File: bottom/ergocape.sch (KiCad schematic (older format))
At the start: 10 parts

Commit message: cleanup and finish the case files
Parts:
- H1, H10, H11, H12, H2, H3, H5, H6, H8, H9: footprint usbc_footprint:mount_hole_2.4x4 -> acheron_MountingHoles:MountingHole_2.5x4.0mm
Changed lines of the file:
@@
 F 0 "H5" H 1100 4996 50  0000 L CNN
 F 1 "MountingHole" H 1100 4905 50  0000 L CNN
-F 2 "usbc_footprint:mount_hole_2.4x4" H 1000 4950 50  0001 C CNN
+F 2 "acheron_MountingHoles:MountingHole_2.5x4.0mm" H 1000 4950 50  0001 C CNN
 F 3 "~" H 1000 4950 50  0001 C CNN
 	1    1000 4950
@@
 F 0 "H12" H 1550 4996 50  0000 L CNN
 F 1 "MountingHole" H 1550 4905 50  0000 L CNN
-F 2 "usbc_footprint:mount_hole_2.4x4" H 1450 4950 50  0001 C CNN
+F 2 "acheron_MountingHoles:MountingHole_2.5x4.0mm" H 1450 4950 50  0001 C CNN
 F 3 "~" H 1450 4950 50  0001 C CNN
 	1    1450 4950
@@
 F 0 "H6" H 1100 5246 50  0000 L CNN
 F 1 "MountingHole" H 1100 5155 50  0000 L CNN
-F 2 "usbc_footprint:mount_hole_2.4x4" H 1000 5200 50  0001 C CNN
+F 2 "acheron_MountingHoles:MountingHole_2.5x4.0mm" H 1000 5200 50  0001 C CNN
 F 3 "~" H 1000 5200 50  0001 C CNN
 	1    1000 5200
@@
 F 0 "H11" H 1550 5246 50  0000 L CNN
 F 1 "MountingHole" H 1550 5155 50  0000 L CNN
-F 2 "usbc_footprint:mount_hole_2.4x4" H 1450 5200 50  0001 C CNN
+F 2 "acheron_MountingHoles:MountingHole_2.5x4.0mm" H 1450 5200 50  0001 C CNN
 F 3 "~" H 1450 5200 50  0001 C CNN
 	1    1450 5200
@@
 F 0 "H10" H 1550 5496 50  0000 L CNN
 F 1 "MountingHole" H 1550 5405 50  0000 L CNN
-F 2 "usbc_footprint:mount_hole_2.4x4" H 1450 5450 50  0001 C CNN
+F 2 "acheron_MountingHoles:MountingHole_2.5x4.0mm" H 1450 5450 50  0001 C CNN
 F 3 "~" H 1450 5450 50  0001 C CNN
 	1    1450 5450
@@
 F 0 "H8" H 1100 5746 50  0000 L CNN
 F 1 "MountingHole" H 1100 5655 50  0000 L CNN
-F 2 "usbc_footprint:mount_hole_2.4x4" H 1000 5700 50  0001 C CNN
+F 2 "acheron_MountingHoles:MountingHole_2.5x4.0mm" H 1000 5700 50  0001 C CNN
 F 3 "~" H 1000 5700 50  0001 C CNN
 	1    1000 5700
@@
 F 0 "H9" H 1550 5746 50  0000 L CNN
 F 1 "MountingHole" H 1550 5655 50  0000 L CNN
-F 2 "usbc_footprint:mount_hole_2.4x4" H 1450 5700 50  0001 C CNN
+F 2 "acheron_MountingHoles:MountingHole_2.5x4.0mm" H 1450 5700 50  0001 C CNN
 F 3 "~" H 1450 5700 50  0001 C CNN
 	1    1450 5700
@@
 F 0 "H1" H 1100 4546 50  0000 L CNN
 F 1 "MountingHole" H 1100 4455 50  0000 L CNN
-F 2 "usbc_footprint:mount_hole_2.4x4" H 1000 4500 50  0001 C CNN
+F 2 "acheron_MountingHoles:MountingHole_2.5x4.0mm" H 1000 4500 50  0001 C CNN
 F 3 "~" H 1000 4500 50  0001 C CNN
 	1    1000 4500
@@
 F 0 "H2" H 1550 4546 50  0000 L CNN
 F 1 "MountingHole" H 1550 4455 50  0000 L CNN
-F 2 "usbc_footprint:mount_hole_2.4x4" H 1450 4500 50  0001 C CNN
+F 2 "acheron_MountingHoles:MountingHole_2.5x4.0mm" H 1450 4500 50  0001 C CNN
 F 3 "~" H 1450 4500 50  0001 C CNN
 	1    1450 4500
@@
 F 0 "H3" H 1100 4796 50  0000 L CNN
 F 1 "MountingHole" H 1100 4705 50  0000 L CNN
-F 2 "usbc_footprint:mount_hole_2.4x4" H 1000 4750 50  0001 C CNN
+F 2 "acheron_MountingHoles:MountingHole_2.5x4.0mm" H 1000 4750 50  0001 C CNN
 F 3 "~" H 1000 4750 50  0001 C CNN
 	1    1000 4750

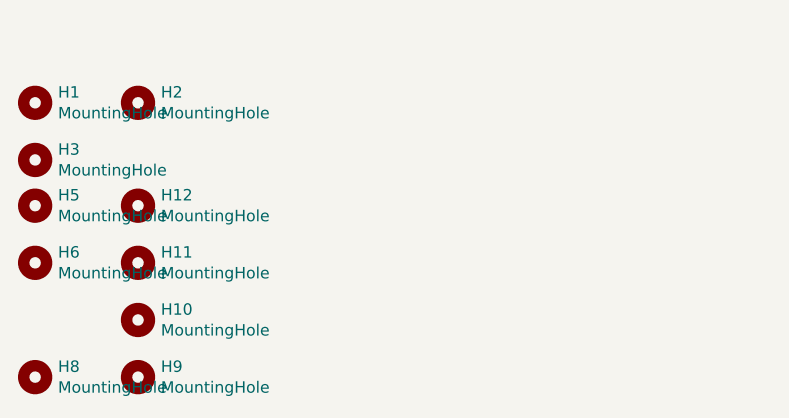
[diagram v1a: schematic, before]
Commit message: finalize plate and mounting holes
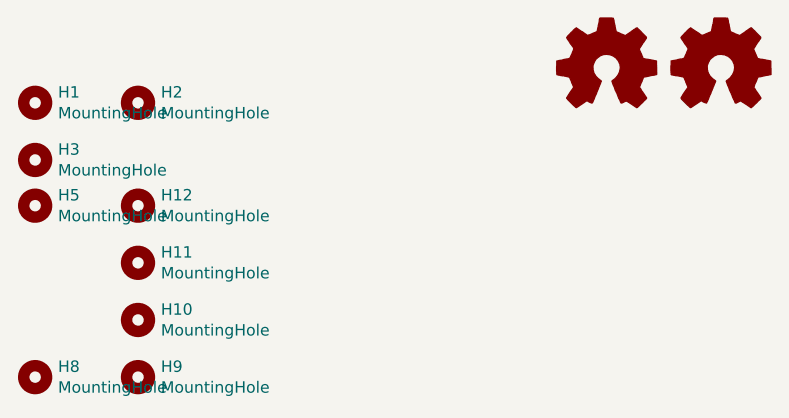
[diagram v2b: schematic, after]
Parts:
- removed H6: MountingHole, acheron_MountingHoles:MountingHole_2.5x4.0mm, symbol Mechanical:MountingHole
- H1, H10, H11, H12, H2, H3, H5, H8, H9: footprint acheron_MountingHoles:MountingHole_2.5x4.0mm -> MountingHole:MountingHole_2.7mm_M2.5
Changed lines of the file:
@@
 EESchema Schematic File Version 4
-LIBS:ergocape-cache
-EELAYER 26 0
+EELAYER 30 0
 EELAYER END
 $Descr A4 11693 8268
@@
 F 0 "H5" H 1100 4996 50  0000 L CNN
 F 1 "MountingHole" H 1100 4905 50  0000 L CNN
-F 2 "acheron_MountingHoles:MountingHole_2.5x4.0mm" H 1000 4950 50  0001 C CNN
+F 2 "MountingHole:MountingHole_2.7mm_M2.5" H 1000 4950 50  0001 C CNN
 F 3 "~" H 1000 4950 50  0001 C CNN
 	1    1000 4950
@@
 F 0 "H12" H 1550 4996 50  0000 L CNN
 F 1 "MountingHole" H 1550 4905 50  0000 L CNN
-F 2 "acheron_MountingHoles:MountingHole_2.5x4.0mm" H 1450 4950 50  0001 C CNN
+F 2 "MountingHole:MountingHole_2.7mm_M2.5" H 1450 4950 50  0001 C CNN
 F 3 "~" H 1450 4950 50  0001 C CNN
 	1    1450 4950
-	1    0    0    -1
-$EndComp
-$Comp
-L Mechanical:MountingHole H6
-U 1 1 5E12F4CE
-P 1000 5200
-F 0 "H6" H 1100 5246 50  0000 L CNN
-F 1 "MountingHole" H 1100 5155 50  0000 L CNN
-F 2 "acheron_MountingHoles:MountingHole_2.5x4.0mm" H 1000 5200 50  0001 C CNN
-F 3 "~" H 1000 5200 50  0001 C CNN
-	1    1000 5200
 	1    0    0    -1
 $EndComp
@@
 F 0 "H11" H 1550 5246 50  0000 L CNN
 F 1 "MountingHole" H 1550 5155 50  0000 L CNN
-F 2 "acheron_MountingHoles:MountingHole_2.5x4.0mm" H 1450 5200 50  0001 C CNN
+F 2 "MountingHole:MountingHole_2.7mm_M2.5" H 1450 5200 50  0001 C CNN
 F 3 "~" H 1450 5200 50  0001 C CNN
 	1    1450 5200
@@
 F 0 "H10" H 1550 5496 50  0000 L CNN
 F 1 "MountingHole" H 1550 5405 50  0000 L CNN
-F 2 "acheron_MountingHoles:MountingHole_2.5x4.0mm" H 1450 5450 50  0001 C CNN
+F 2 "MountingHole:MountingHole_2.7mm_M2.5" H 1450 5450 50  0001 C CNN
 F 3 "~" H 1450 5450 50  0001 C CNN
 	1    1450 5450
@@
 F 0 "H8" H 1100 5746 50  0000 L CNN
 F 1 "MountingHole" H 1100 5655 50  0000 L CNN
-F 2 "acheron_MountingHoles:MountingHole_2.5x4.0mm" H 1000 5700 50  0001 C CNN
+F 2 "MountingHole:MountingHole_2.7mm_M2.5" H 1000 5700 50  0001 C CNN
 F 3 "~" H 1000 5700 50  0001 C CNN
 	1    1000 5700
@@
 F 0 "H9" H 1550 5746 50  0000 L CNN
 F 1 "MountingHole" H 1550 5655 50  0000 L CNN
-F 2 "acheron_MountingHoles:MountingHole_2.5x4.0mm" H 1450 5700 50  0001 C CNN
+F 2 "MountingHole:MountingHole_2.7mm_M2.5" H 1450 5700 50  0001 C CNN
 F 3 "~" H 1450 5700 50  0001 C CNN
 	1    1450 5700
@@
 F 0 "H1" H 1100 4546 50  0000 L CNN
 F 1 "MountingHole" H 1100 4455 50  0000 L CNN
-F 2 "acheron_MountingHoles:MountingHole_2.5x4.0mm" H 1000 4500 50  0001 C CNN
+F 2 "MountingHole:MountingHole_2.7mm_M2.5" H 1000 4500 50  0001 C CNN
 F 3 "~" H 1000 4500 50  0001 C CNN
 	1    1000 4500
@@
 F 0 "H2" H 1550 4546 50  0000 L CNN
 F 1 "MountingHole" H 1550 4455 50  0000 L CNN
-F 2 "acheron_MountingHoles:MountingHole_2.5x4.0mm" H 1450 4500 50  0001 C CNN
+F 2 "MountingHole:MountingHole_2.7mm_M2.5" H 1450 4500 50  0001 C CNN
 F 3 "~" H 1450 4500 50  0001 C CNN
 	1    1450 4500
@@
 F 0 "H3" H 1100 4796 50  0000 L CNN
 F 1 "MountingHole" H 1100 4705 50  0000 L CNN
-F 2 "acheron_MountingHoles:MountingHole_2.5x4.0mm" H 1000 4750 50  0001 C CNN
+F 2 "MountingHole:MountingHole_2.7mm_M2.5" H 1000 4750 50  0001 C CNN
 F 3 "~" H 1000 4750 50  0001 C CNN
 	1    1000 4750
 	1    0    0    -1
 $EndComp
+$Comp
+L Graphic:Logo_Open_Hardware_Small #LOGO1
+U 1 1 5E22B141
+P 3500 4350
+F 0 "#LOGO1" H 3500 4625 50  0001 C CNN
+F 1 "Logo_Open_Hardware_Small" H 3500 4125 50  0001 C CNN
+F 2 "" H 3500 4350 50  0001 C CNN
+F 3 "~" H 3500 4350 50  0001 C CNN
+	1    3500 4350
+	1    0    0    -1
+$EndComp
+$Comp
+L Graphic:Logo_Open_Hardware_Small #LOGO2
+U 1 1 5E22BDC7
+P 4000 4350
+F 0 "#LOGO2" H 4000 4625 50  0001 C CNN
+F 1 "Logo_Open_Hardware_Small" H 4000 4125 50  0001 C CNN
+F 2 "" H 4000 4350 50  0001 C CNN
+F 3 "~" H 4000 4350 50  0001 C CNN
+	1    4000 4350
+	1    0    0    -1
+$EndComp
